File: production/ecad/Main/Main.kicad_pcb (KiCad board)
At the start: 4 copper layers, 59.5 x 82.5 mm, 43 parts, among them J1 214721-0061, J10 214721-0061, J11 2147210040, J2 214721-0100, J3 214721-0080, J4 214721-0020, J5 214721-0020, J6 214721-0020, J7 ADC-028-1-T/R-PA10T, J8 61301611821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

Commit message: errors
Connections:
- net /Load_Cell_and_Amplifier/AVDD renamed AVDD
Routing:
- net GND: track 259.4 -> 269.4 mm, vias 27 -> 28
- net AVDD: track 37.8 -> 44.8 mm, vias 0 -> 2
- net 5VEXT: track 213.1 -> 215.1 mm
- net Net-(J6-Pad2): track 12.0 -> 12.7 mm

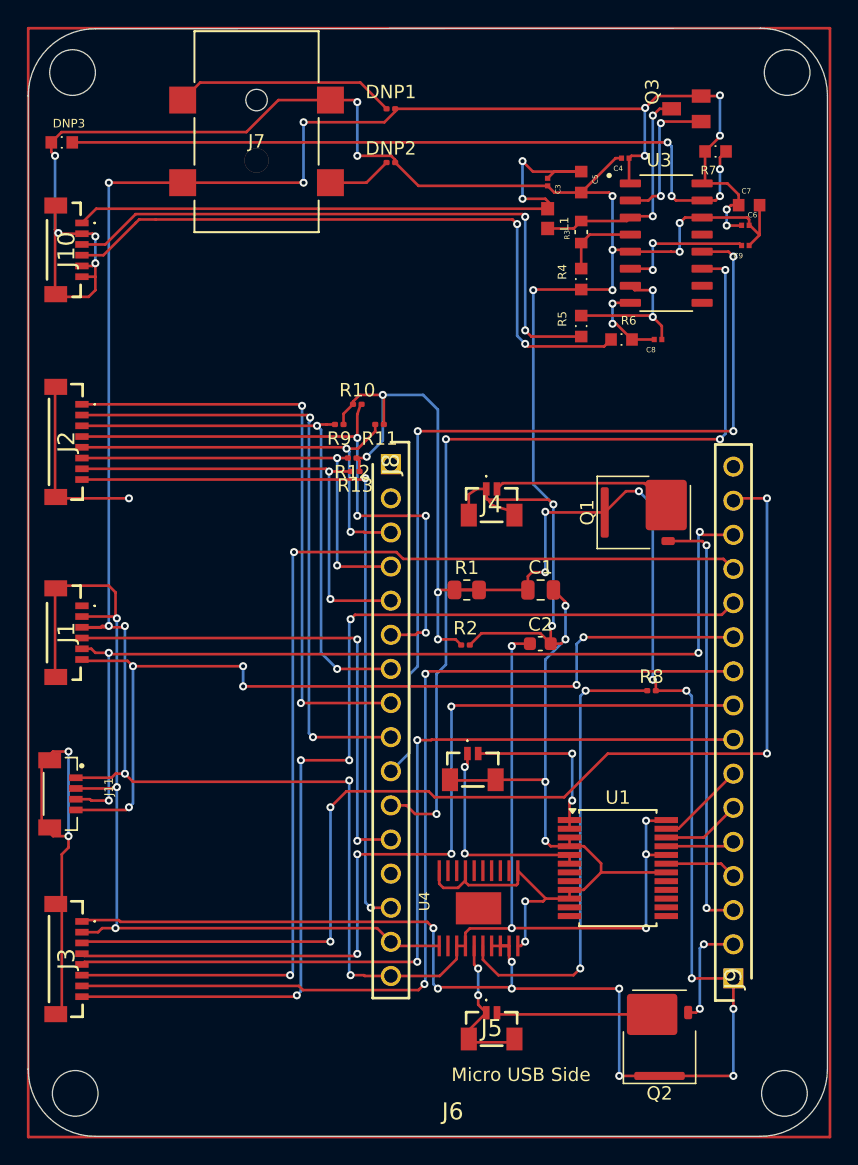
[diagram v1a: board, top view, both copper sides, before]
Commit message: downsized board
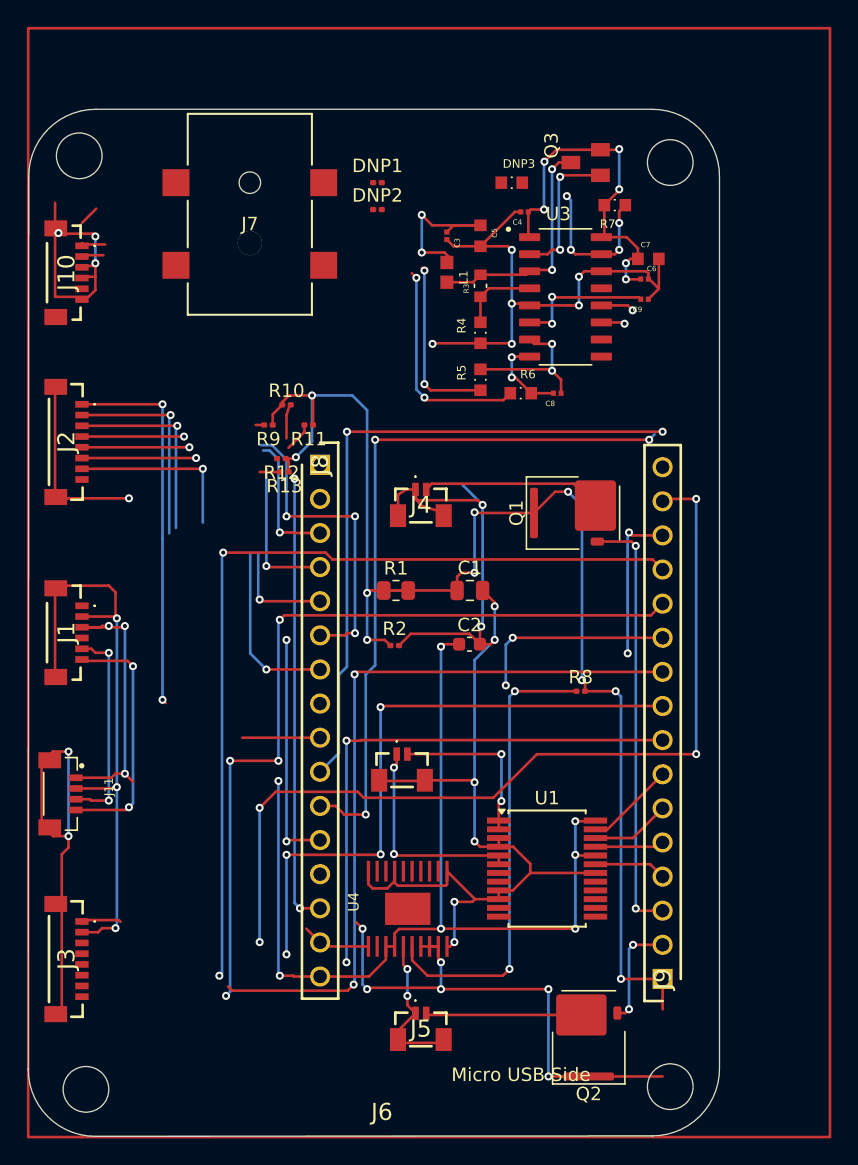
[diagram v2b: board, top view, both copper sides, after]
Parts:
- moved DNP3 33.6 mm to (86.0, 61.0)
- moved C3 8.50 mm to (81.2, 65.0)
- moved C4 8.50 mm to (87.0, 63.2)
- moved C5 8.50 mm to (83.7, 65.0)
- moved C6 8.50 mm to (95.9, 68.2)
- moved C7 8.50 mm to (96.2, 66.7)
- moved C8 8.50 mm to (89.4, 76.7)
- moved C9 8.50 mm to (95.9, 69.7)
- moved L1 8.50 mm to (81.2, 67.7)
- moved Q3 8.50 mm to (91.5, 59.5)
- moved R3 8.50 mm to (83.7, 68.7)
- moved R4 8.50 mm to (83.7, 72.2)
- moved R5 8.50 mm to (83.7, 75.7)
- moved R6 8.50 mm to (86.7, 76.7)
- moved R7 8.50 mm to (93.7, 62.7)
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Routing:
- net 5VEXT: track 215.1 -> 121.2 mm, vias 19 -> 16
- net GND: track 269.4 -> 187.1 mm, vias 28 -> 25
- net Net-(U3-RATE): track 55.8 -> 11.5 mm
- net SCL: track 71.6 -> 27.9 mm
- net SDA: track 68.6 -> 34.1 mm, vias 6 -> 4
- net /Load_Cell_and_Amplifier/A-: track 47.0 -> 13.1 mm
- net /Load_Cell_and_Amplifier/A+: track 49.5 -> 16.3 mm
- net AVDD: track 44.8 -> 13.1 mm
- net 3V3EXT: track 174.9 -> 147.1 mm, vias 18 -> 16
- net ANO_ENCB: track 46.8 -> 21.2 mm, vias 2 -> 1
- net LCD_CS: track 65.1 -> 40.3 mm
- net ANO_COMA: track 54.8 -> 33.8 mm
- net IMU_VOUT: track 38.1 -> 17.7 mm
- net LCD_CLK: track 67.1 -> 46.9 mm
- net ANO_ENCA: track 45.3 -> 28.3 mm
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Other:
- board size 59.5 x 82.5 mm -> 51.5 x 76.5 mm

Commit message: Routing updated
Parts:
- moved C3 1.00 mm to (82.2, 65.0)
- moved C4 1.00 mm to (88.0, 63.2)
- moved C5 1.00 mm to (84.7, 65.0)
- moved C6 1.00 mm to (96.9, 68.2)
- moved C7 1.00 mm to (97.2, 66.7)
- moved C8 1.00 mm to (90.4, 76.7)
- moved C9 1.00 mm to (96.9, 69.7)
- moved DNP3 1.00 mm to (87.0, 61.0)
- moved L1 1.00 mm to (82.2, 67.7)
- moved Q3 1.00 mm to (92.5, 59.5)
- moved R3 1.00 mm to (84.7, 68.7)
- moved R4 1.00 mm to (84.7, 72.2)
- moved R5 1.00 mm to (84.7, 75.7)
- moved R6 1.00 mm to (87.7, 76.7)
- moved R7 1.00 mm to (94.7, 62.7)
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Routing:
- net 5VEXT: track 121.2 -> 165.8 mm, vias 16 -> 19
- net GND: track 187.1 -> 218.0 mm
- net ANO_SW2: track 16.8 -> 47.1 mm
- net /Load_Cell_and_Amplifier/A+: track 16.3 -> 43.5 mm, vias 2 -> 4
- net /Load_Cell_and_Amplifier/A-: track 13.1 -> 39.4 mm
- net AVDD: track 13.1 -> 38.0 mm
- net ANO_ENCB: track 21.2 -> 41.7 mm, vias 1 -> 2
- net Net-(DNP1-Pad1): track 0.00 -> 17.5 mm, vias 0 -> 2
- net ANO_COMA: track 33.8 -> 49.9 mm
- net ANO_SW1: track 28.7 -> 44.4 mm
- net ANO_SW3: track 20.1 -> 34.3 mm, vias 2 -> 3
- net ANO_ENCA: track 28.3 -> 39.8 mm
- net W_DAT: track 52.2 -> 60.0 mm
- net Net-(DNP2-Pad1): track 0.00 -> 7.64 mm, vias 0 -> 2
- net W_SCK: track 54.6 -> 62.0 mm
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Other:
- outline, holes or cut-outs redrawn

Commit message: Final changes updated
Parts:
- added ?: LOGO, LOGO, F.Cu at (62.5, 101.0)
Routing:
- net SCL: track 27.9 -> 67.7 mm
- net SDA: track 34.1 -> 62.0 mm
- net LCD_CS: track 40.3 -> 60.1 mm
- net 3V3EXT: track 146.0 -> 163.8 mm
- net IMU_VOUT: track 17.7 -> 33.0 mm
- net LCD_CLK: track 46.9 -> 62.2 mm
- net LCD_DIN: track 34.5 -> 47.8 mm
- net LCD_RST: track 55.8 -> 66.7 mm
- net LCD_BL: track 60.9 -> 71.7 mm
- net LCD_DS: track 64.9 -> 75.1 mm
- net 5VEXT: track 165.8 -> 174.7 mm, vias 19 -> 18
- net GND: track 218.0 -> 218.8 mm, vias 25 -> 27
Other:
- board text added: "Design by: Neha Joby Max Langweil Will Fox David Abrahamyan Chris Georges"
- board text added: "FITOLUX"
- board text added: "Fitolux Main Board : v1p0"

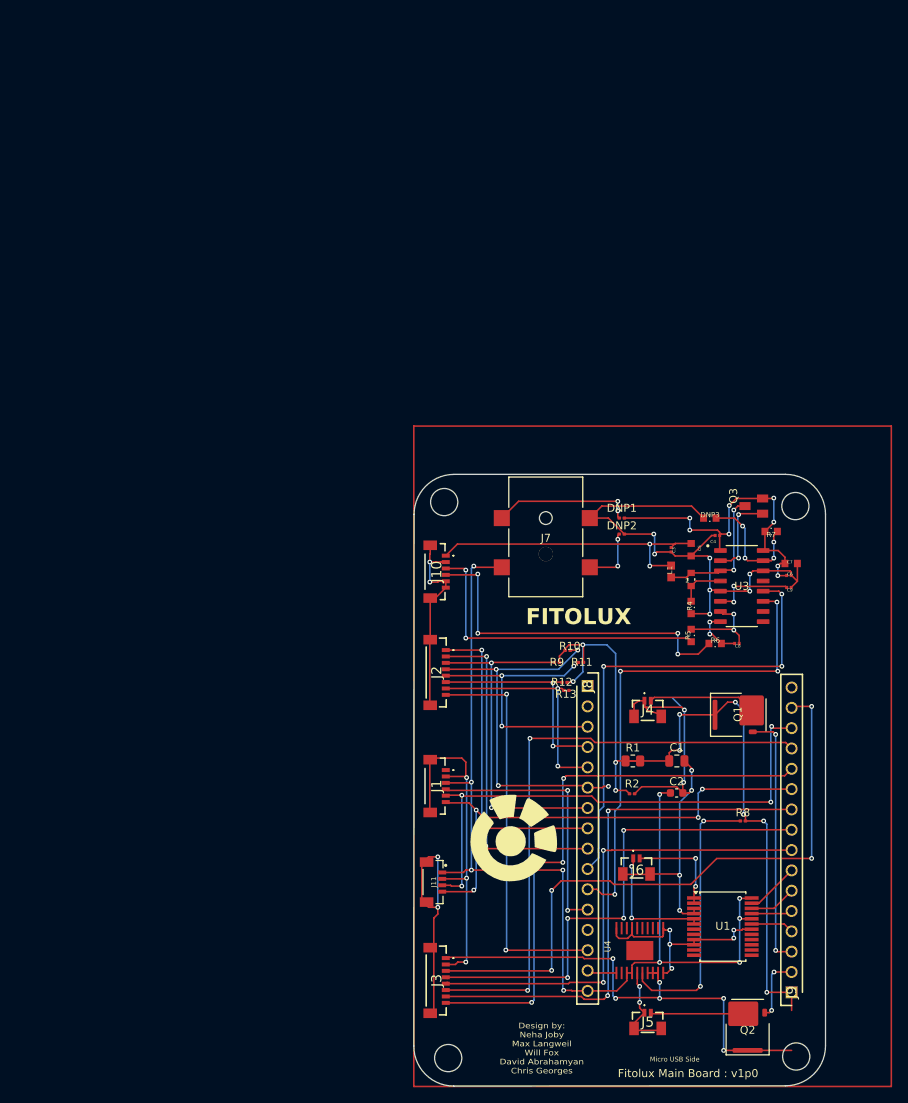
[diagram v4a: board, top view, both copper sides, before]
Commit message: Added 3V3, 5V, and GND power planes on layer 2
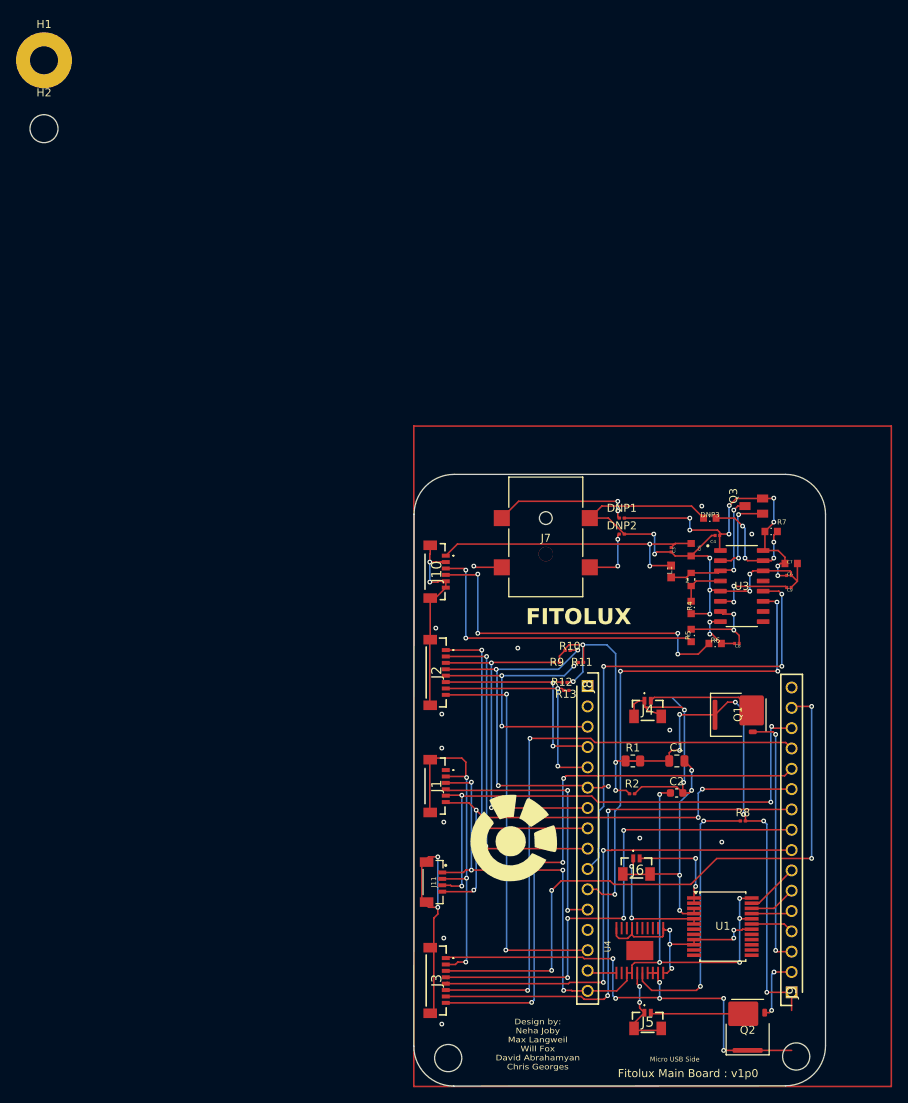
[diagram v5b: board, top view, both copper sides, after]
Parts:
- added H1: MountingHole_Pad, MountingHole:MountingHole_3.5mm_Pad, F.Cu at (3.77, 3.77)
- added H2: MountingHole, MountingHole:MountingHole_3.5mm, F.Cu at (3.77, 12.3)
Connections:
- net AVDD renamed /Load_Cell_and_Amplifier/AVDD
- U4 pad P$21: (no net) -> GND
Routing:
- net 5VEXT: track 174.7 -> 147.6 mm
- net GND: vias 27 -> 39
- added copper zone on In1.Cu, net GND
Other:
- outline, holes or cut-outs redrawn
